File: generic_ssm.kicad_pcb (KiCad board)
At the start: 4 copper layers, 98 x 84 mm, 21 parts, among them J1 RST_JMP, J2 DEBUG CONN, J3 PROGRAMMING PORT, SW1 SW_RST, U1 SN65HVD230, U2 ATMEGA32M1-MU, Y1 8MHz

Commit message: Bugfixes to the PCB layout.
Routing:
- net GND: track 31.2 -> 31.8 mm
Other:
- board text added: "3V3 NCRT"
- board text removed: "3V3 CRT"

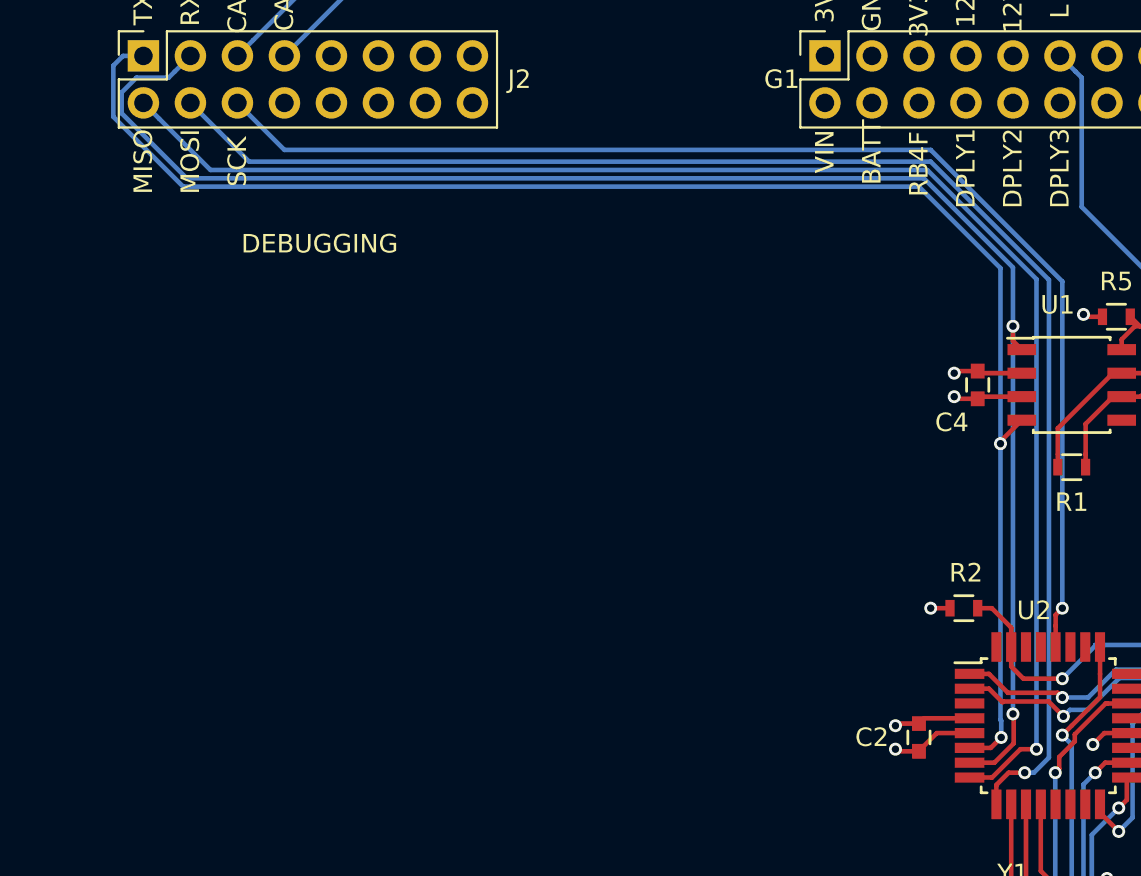
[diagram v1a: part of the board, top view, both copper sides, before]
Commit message: Updated PCB schematic with CAN fixes.
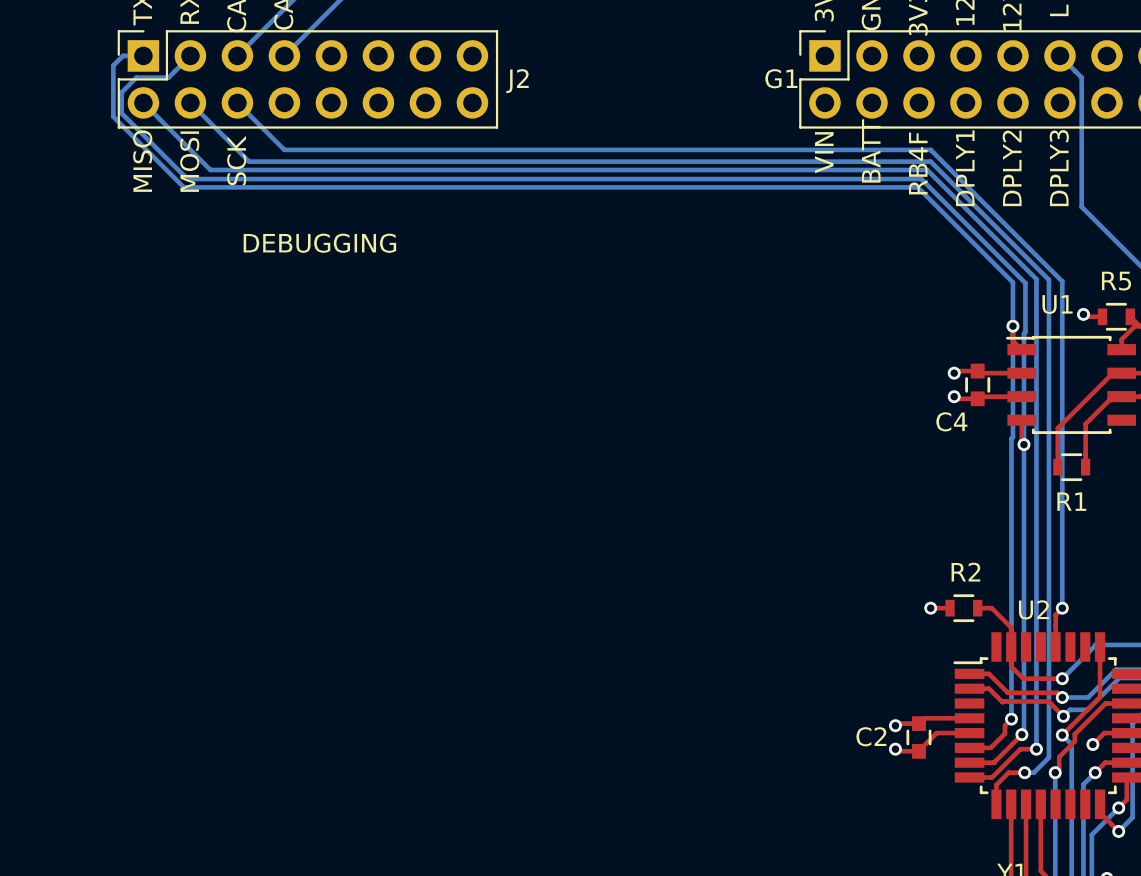
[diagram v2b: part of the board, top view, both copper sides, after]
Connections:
- U1 pad 1: /RX_CAN -> /TX_CAN
- U1 pad 4: /TX_CAN -> /RX_CAN
- U1 pad 6: /CANH -> /CANL
- U1 pad 7: /CANL -> /CANH
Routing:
- net /CANL: track 90.1 -> 107.7 mm
- net /CANH: track 93.1 -> 75.5 mm
- net /RX_CAN: track 87.3 -> 87.9 mm
